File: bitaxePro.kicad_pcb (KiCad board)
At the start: 4 copper layers, 87.7 x 62.9 mm, 91 parts, among them IC1 BM1397_mode1, J1 Conn_01x01, J2 Conn_01x01, J3 Conn_01x05, J4 Conn_01x02, J5 Conn_01x03, U1 SN74LVC1T45DRLR, U2 oscillator, U3 SN74LVC1T45DRLR, U4 SN74LVC1T45DRLR, U5 MCP1824, U6 MCP1824, U7 ESP32-C3-DEVKITC-02, U8 NCT218

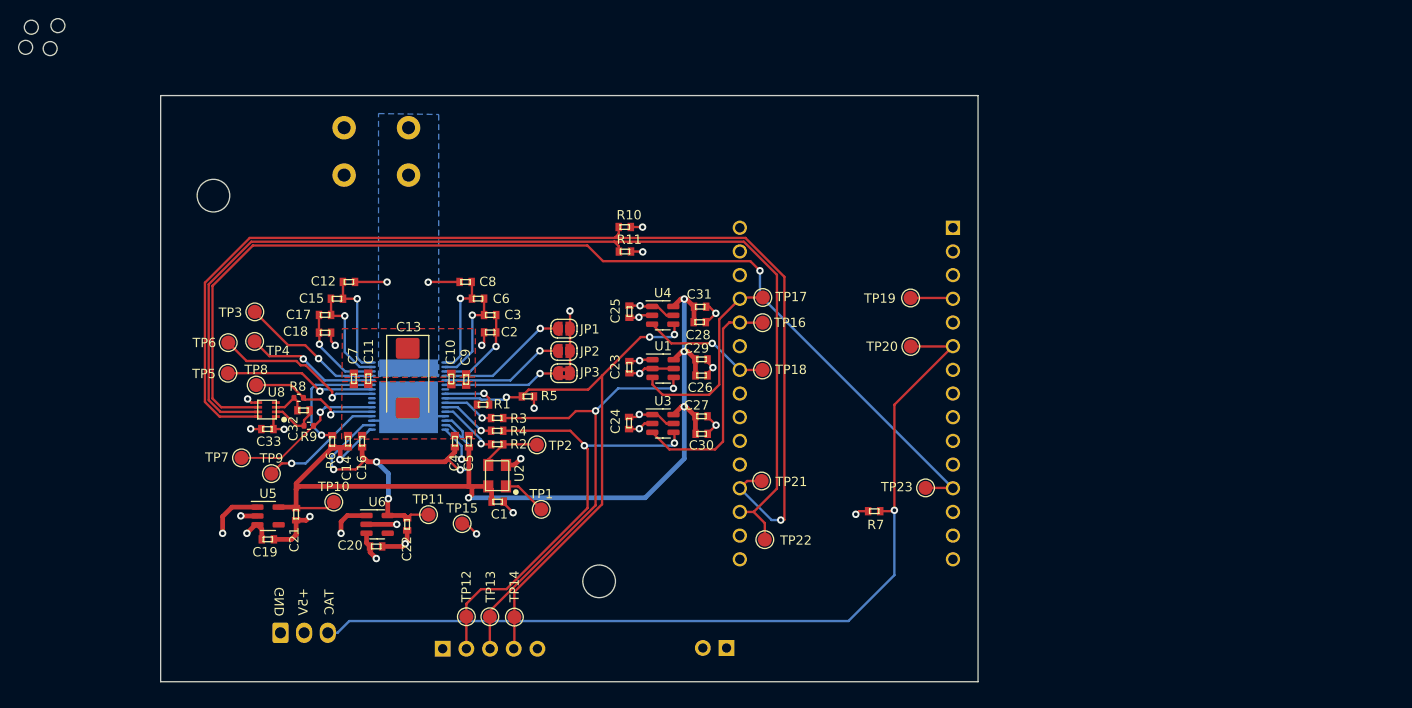
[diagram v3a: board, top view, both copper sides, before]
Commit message: routing cleanup
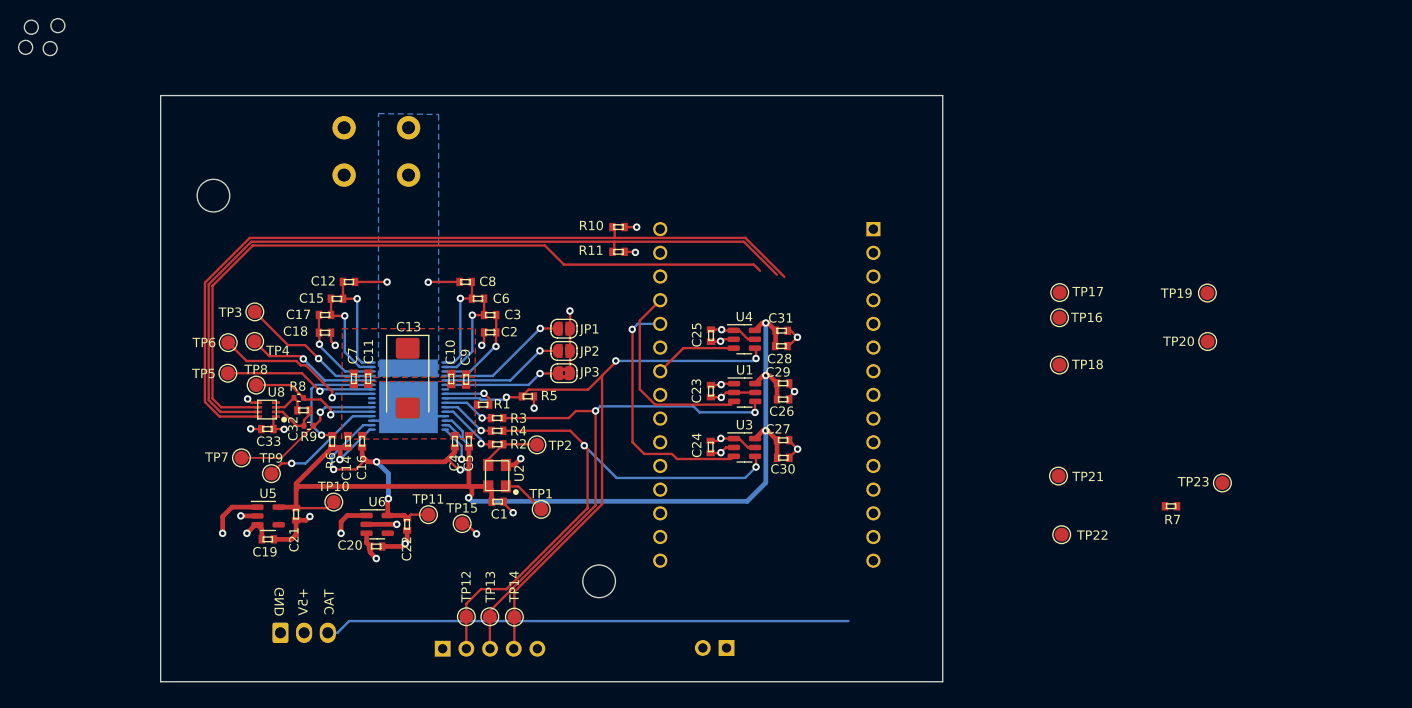
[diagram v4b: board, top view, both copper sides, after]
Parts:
- removed kibuzzard-62B6C053: G***, kibuzzard-62B6C053
- added kibuzzard-62B6C6A5: G***, kibuzzard-62B6C6A5, B.Cu at (112.7, 51.0)
- moved TP16 31.8 mm to (159.1, 69.0)
- moved R7 31.8 mm to (171.1, 89.2)
- moved TP18 31.8 mm to (159.1, 74.1)
- moved TP19 31.8 mm to (175.0, 66.4)
- moved TP20 31.8 mm to (175.0, 71.6)
- moved TP21 31.8 mm to (159.0, 86.0)
- moved TP22 31.8 mm to (159.3, 92.3)
- moved TP23 31.8 mm to (176.6, 86.7)
- moved TP17 31.8 mm to (159.1, 66.3)
- moved C26 9.12 mm to (129.5, 77.8)
- moved C28 9.12 mm to (129.3, 72.1)
- moved C27 9.12 mm to (129.5, 82.2)
- moved C29 9.12 mm to (129.5, 76.0)
- moved C23 9.12 mm to (121.7, 76.9)
- moved U1 9.12 mm to (125.3, 77.0)
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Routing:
- net /FAN_TACH: track 96.6 -> 56.4 mm, vias 1 -> 0
- net /SCL: track 121.3 -> 86.3 mm, vias 1 -> 0
- net /TEMP_ALRT: track 113.9 -> 79.0 mm, vias 1 -> 0
- net /SDA: track 115.2 -> 83.7 mm
- net /CI: track 49.3 -> 59.9 mm
- net /RO: track 51.0 -> 59.2 mm
- net /1V8: track 111.3 -> 119.3 mm
- net /RST_N: track 61.9 -> 69.8 mm
- net /RST: track 13.9 -> 8.90 mm, vias 1 -> 0
- net Net-(U7-Pad4): track 4.59 -> 0.00 mm
- net /TX: track 25.3 -> 27.1 mm, vias 0 -> 1
- net /VCCIO: track 19.6 -> 18.1 mm, vias 7 -> 6
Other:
- board size 87.7 x 62.9 mm -> 83.9 x 62.9 mm

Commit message: updated readme, finished routing
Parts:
- moved H3 114.0 mm to (141.9, 103.7)
- moved H4 94.4 mm to (142.1, 49.7)
- moved H5 65.8 mm to (66.3, 104.1)
- moved TP16 43.8 mm to (118.8, 86.3)
- moved TP17 42.6 mm to (118.8, 80.2)
- moved TP23 40.8 mm to (135.9, 89.4)
- moved TP18 39.2 mm to (119.9, 74.0)
- moved TP20 38.8 mm to (136.2, 72.2)
- moved TP19 38.8 mm to (136.2, 67.2)
- moved R7 37.8 mm to (135.9, 75.5)
- moved TP21 33.5 mm to (125.9, 91.2)
- moved TP22 33.4 mm to (126.0, 94.3)
- moved H6 18.9 mm to (66.8, 49.0)
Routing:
- net /SDA: track 83.7 -> 131.7 mm, vias 0 -> 1
- net /SCL: track 86.3 -> 134.0 mm, vias 0 -> 1
- net /TEMP_ALRT: track 79.0 -> 114.0 mm, vias 0 -> 1
- net /FAN_TACH: track 56.4 -> 90.1 mm
- net /5V: track 120.9 -> 111.2 mm
- net Net-(U7-Pad4): track 0.00 -> 2.95 mm
- net /TX: track 27.1 -> 29.9 mm
- net /RX: track 21.4 -> 24.1 mm
- net /VCCIO: track 18.1 -> 19.9 mm, vias 6 -> 7
- net /RST: track 8.90 -> 10.6 mm
- net GND: vias 19 -> 35
- net /VDD: vias 2 -> 8
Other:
- outline, holes or cut-outs redrawn

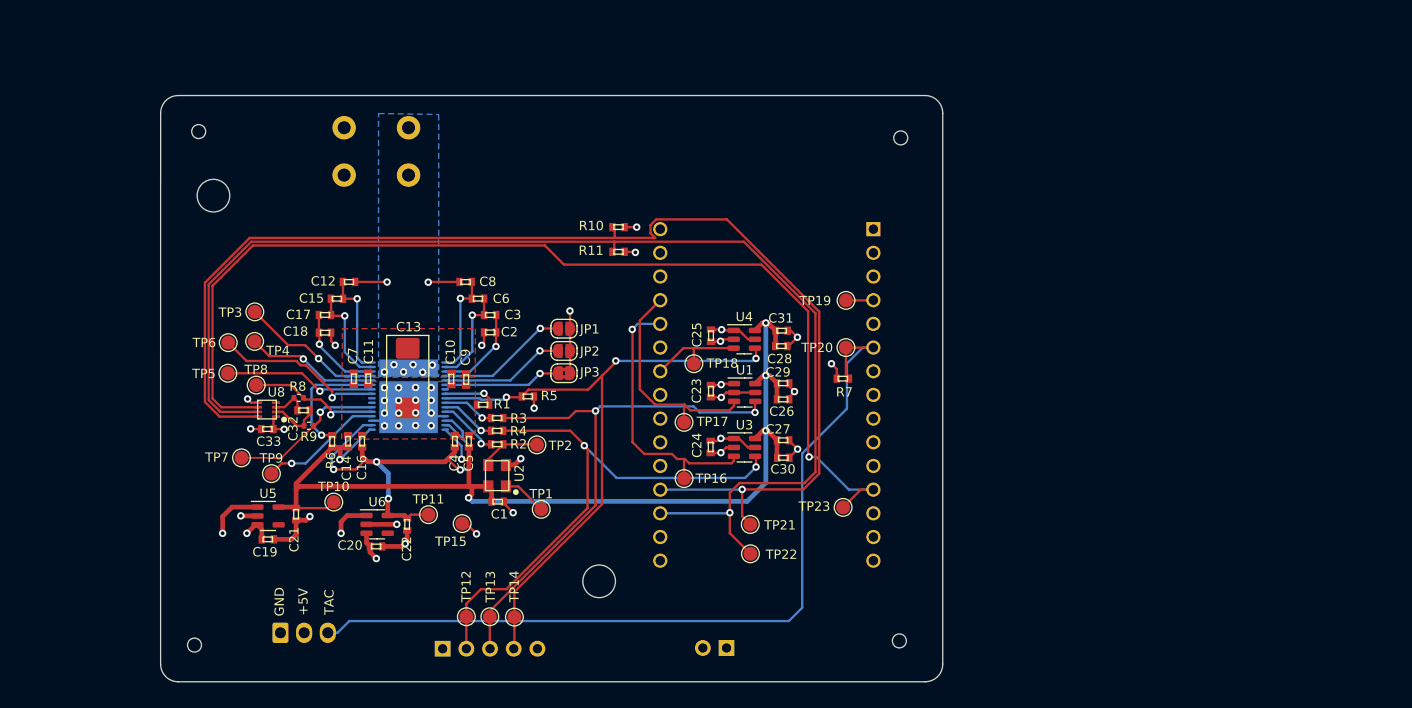
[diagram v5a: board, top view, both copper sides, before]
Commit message: switched out some OOS parts, generated BOM
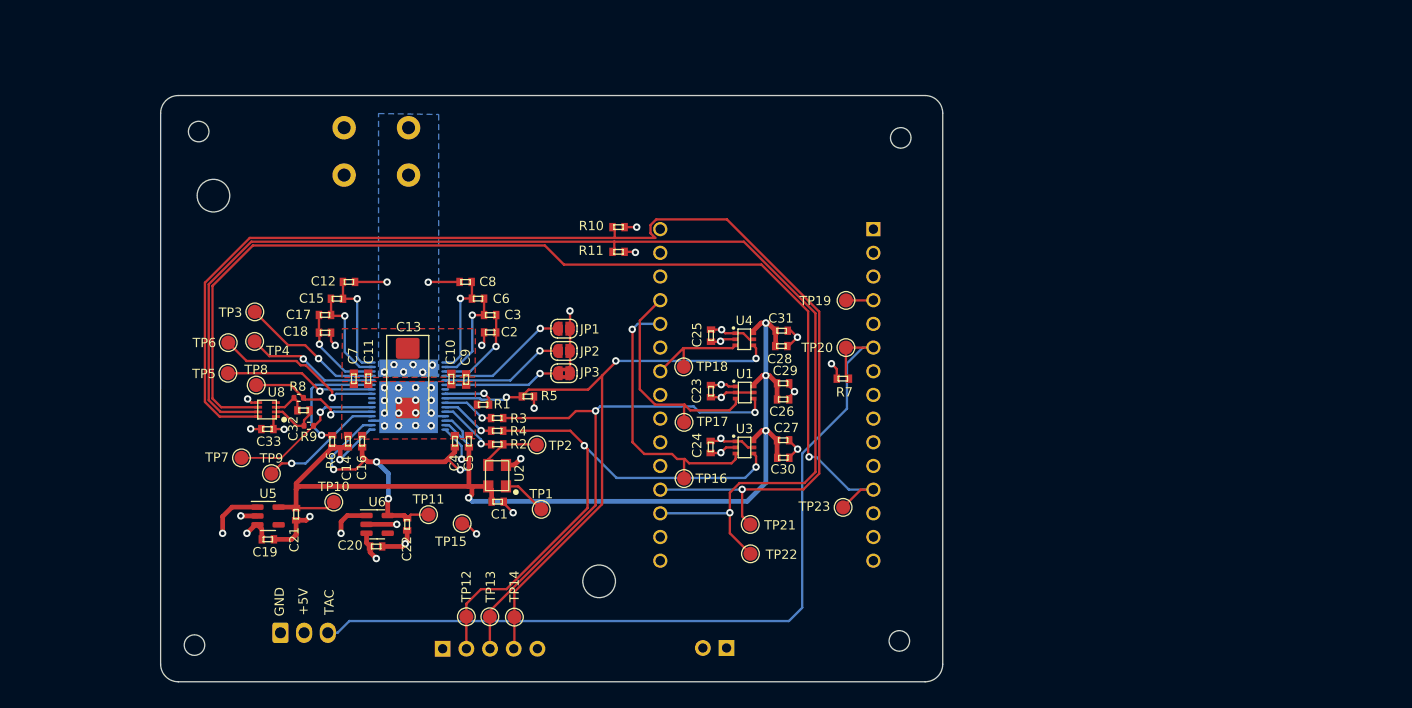
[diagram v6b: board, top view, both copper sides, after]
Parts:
- H3, H4, H5, H6: footprint DayMiner:alignment_pin_1.5mm -> MountingHole:MountingHole_2.2mm_M2
- U1, U3, U4: value SN74LVC1T45DRLR -> SN74LVC1T45QDCKRQ1; footprint Package_TO_SOT_SMD:SOT-23-6 -> Package_TO_SOT_SMD:SOT-363_SC-70-6
- moved TP18 1.14 mm to (118.8, 74.3)
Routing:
- net /1V8: track 119.3 -> 120.0 mm
- net /RST: track 10.6 -> 11.2 mm
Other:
- board text added: "R1"
- board text added: "RX"
- board text added: "SCL"
- board text added: "SDA"
- board text added: "TX"
